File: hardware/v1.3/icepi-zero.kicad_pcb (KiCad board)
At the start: 4 copper layers, 65 x 30 mm, 161 parts, among them J1 Conn_02x20_Counter_Clockwise, J2 HDMI_C_1.3, J3 USB_C_Receptacle_USB2.0_14P, J4 USB_C_Receptacle_USB2.0_14P, J5 USB_C_Receptacle_USB2.0_14P, J6 Micro_SD_Card_Det2, SW1 SW_Push, SW2 SW_Push, U1 ECP5-CABGA256, U10 W9825G6KH, U11 W25Q128JVS, U2 TLV62569DBV, U3 TLV62569DBV, U4 TLV62569DBV, U5 PCA9306DC1, U6 FT231XQ, U7 TPD2EUSB30A, U8 TPD2EUSB30A, U9 TPD2EUSB30A, Y1 SG-8018CG 50.000000MHz

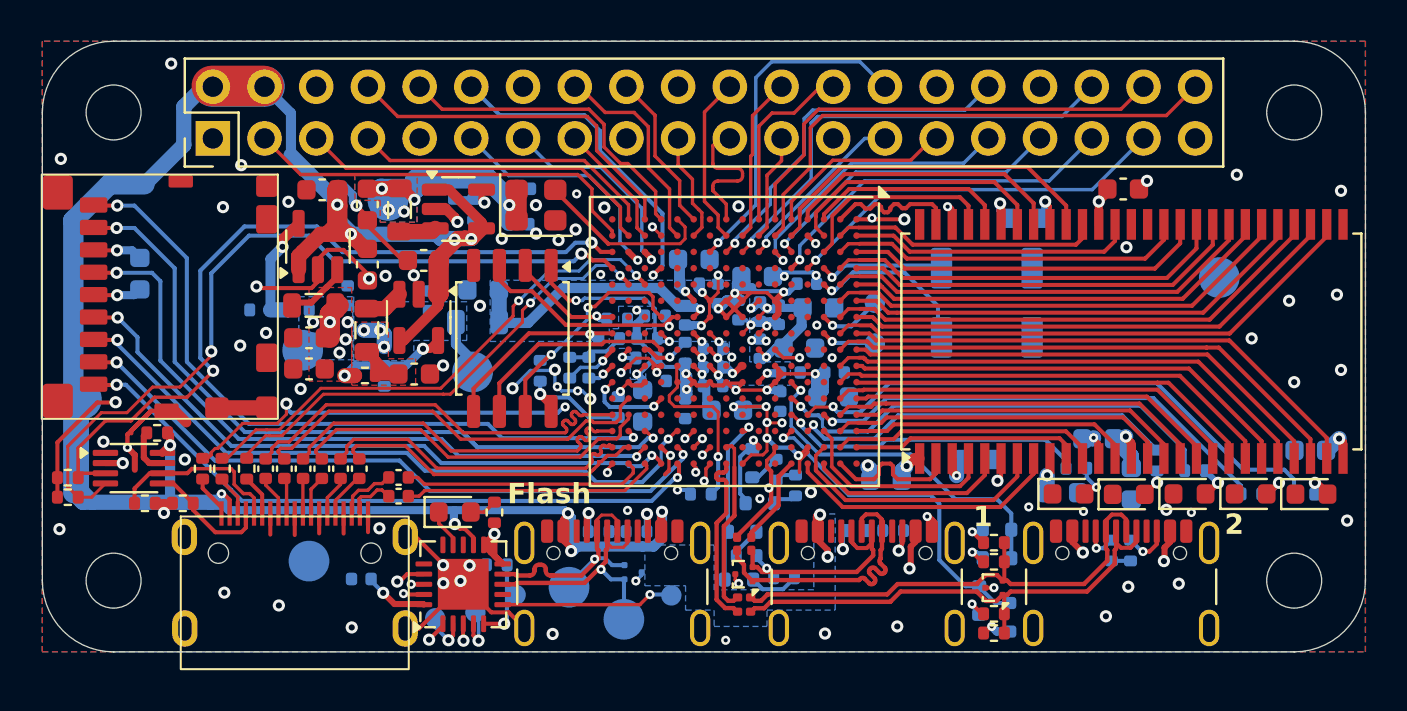
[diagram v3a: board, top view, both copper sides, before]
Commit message: Added start of documentation and changed GPDI
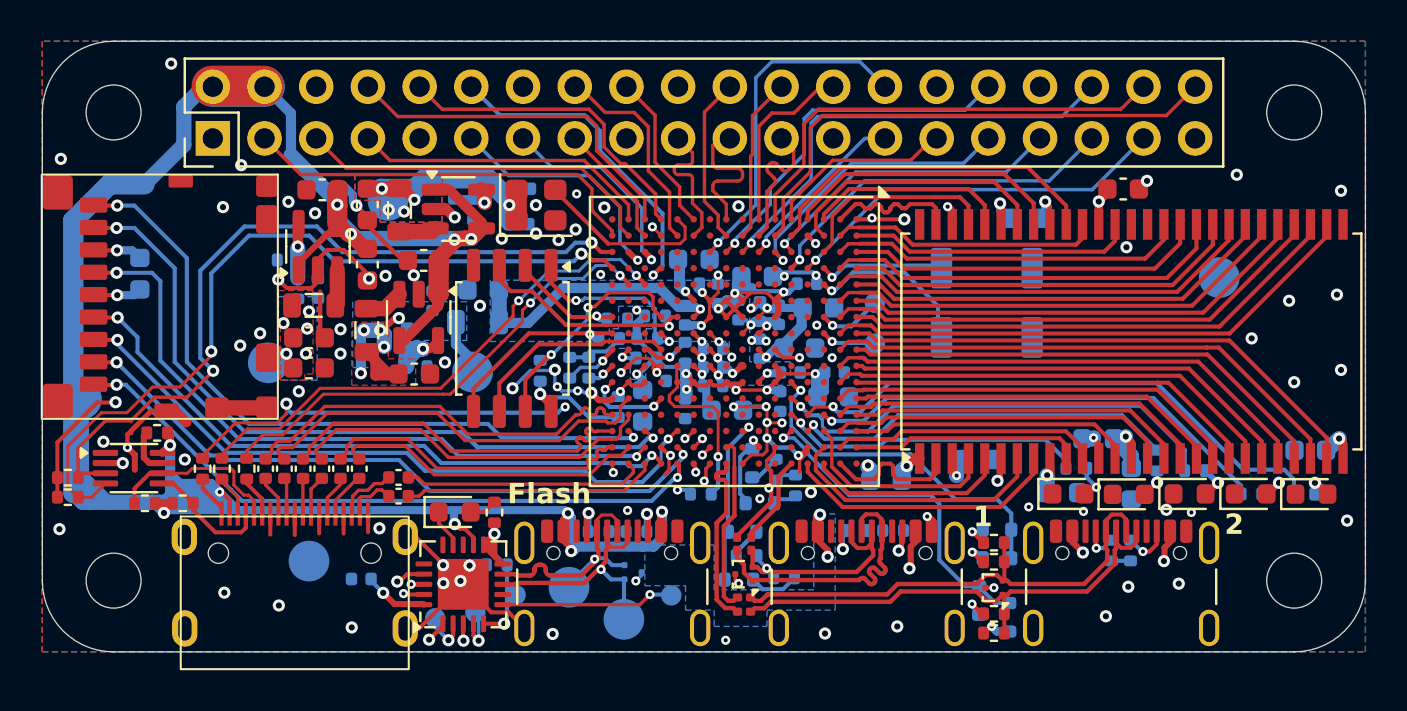
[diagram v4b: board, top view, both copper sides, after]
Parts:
- added REF**: CE-Logo_8.5x6mm_SilkScreen, Symbol:CE-Logo_8.5x6mm_SilkScreen, B.Cu at (126.6, 99.5)
- J2: value HDMI_C_1.3 -> GPDI_C_1.3
- R8: moved to B.Cu
- moved R7 2.80 mm to (128.1, 100.8)
- moved R8 2.77 mm to (133.9, 104.6), turned to -90 degrees
- moved TP6 1.80 mm to (127.1, 105.8)
- moved R9 1.65 mm to (134.4, 106.0), turned to 0 degrees
- moved C7 1.50 mm to (129.5, 102.1)
- moved R6 1.05 mm to (128.6, 102.2), turned to 90 degrees
- moved C19 0.17 mm to (135.2, 102.8)
- turned C6 to 0 degrees
- turned C5 to 0 degrees
- turned L1 to 180 degrees
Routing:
- net +5V: track 172.3 -> 189.5 mm
- net +2V5: track 8.96 -> 12.3 mm, vias 3 -> 5
- net Net-(U2-FB): track 5.70 -> 2.57 mm
- net +1V1: track 40.8 -> 38.3 mm
- net Net-(U3-FB): track 5.80 -> 3.96 mm, vias 2 -> 1
- net /GPIO11: track 5.24 -> 7.00 mm
- net /GPIO10: track 5.42 -> 6.85 mm
- net GND: track 98.4 -> 99.5 mm, vias 108 -> 111
- net Net-(U2-SW): track 2.62 -> 1.80 mm
- net /GPDI/GPDI_CLK-: track 20.5 -> 19.9 mm

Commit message: DVI multires
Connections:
- U1 pad M11: /USB/JTAG_TDO -> unconnected-(U1E-PR47A/+/HS/RSQ44-PadM11)
- U1 pad N12: /USB/JTAG_TMS -> unconnected-(U1E-PR44D/-/RSQ44-PadN12)
- U1 pad P11: /USB/JTAG_TDI -> unconnected-(U1E-PR47C/+/RSQ44/LRC_GPLL0T_IN-PadP11)
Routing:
- net /USB/JTAG_TDI: track 32.6 -> 31.7 mm
- net /USB/JTAG_TMS: track 34.5 -> 34.0 mm
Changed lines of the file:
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@@
 	(net 259 "/GPIO27")
 	(net 260 "unconnected-(U1J-PB18A{slash}WRITEN-PadM9)")
+	(net 261 "unconnected-(U1E-PR44D{slash}-{slash}RSQ44-PadN12)")
+	(net 262 "unconnected-(U1E-PR47C{slash}+{slash}RSQ44{slash}LRC_GPLL0T_IN-PadP11)")
+	(net 263 "unconnected-(U1E-PR47A{slash}+{slash}HS{slash}RSQ44-PadM11)")
 	(footprint "MountingHole:MountingHole_2.7mm_M2.5"
 		(layer "F.Cu")
@@
 			(property pad_prop_bga)
 			(layers "F.Cu" "F.Mask" "F.Paste")
-			(net 5 "/USB/JTAG_TDO")
+			(net 263 "unconnected-(U1E-PR47A{slash}+{slash}HS{slash}RSQ44-PadM11)")
 			(pinfunction "PR47A/+/HS/RSQ44")
 			(pintype "bidirectional")
@@
 			(property pad_prop_bga)
 			(layers "F.Cu" "F.Mask" "F.Paste")
-			(net 8 "/USB/JTAG_TMS")
+			(net 261 "unconnected-(U1E-PR44D{slash}-{slash}RSQ44-PadN12)")
 			(pinfunction "PR44D/-/RSQ44")
 			(pintype "bidirectional")
@@
 			(property pad_prop_bga)
 			(layers "F.Cu" "F.Mask" "F.Paste")
-			(net 4 "/USB/JTAG_TDI")
+			(net 262 "unconnected-(U1E-PR47C{slash}+{slash}RSQ44{slash}LRC_GPLL0T_IN-PadP11)")
 			(pinfunction "PR47C/+/RSQ44/LRC_GPLL0T_IN")
 			(pintype "bidirectional")
@@
 		(net 4)
 	)
-	(segment
-		(start 144.96 106.91)
-		(end 144.8 106.75)
-		(width 0.2)
-		(layer "F.Cu")
-		(net 4)
-	)
-	(segment
-		(start 145.44 106.91)
-		(end 144.96 106.91)
-		(width 0.2)
-		(layer "F.Cu")
-		(net 4)
-	)
-	(segment
-		(start 145.6 106.75)
-		(end 145.44 106.91)
-		(width 0.2)
-		(layer "F.Cu")
-		(net 4)
-	)
 	(via
 		(at 144.399998 107.209961)
@@
 	)
 	(segment
-		(start 148.931745 107.95)
-		(end 149.199998 108.218253)
+		(start 147.19 105.95)
+		(end 146.8 106.34)
 		(width 0.15)
 		(layer "F.Cu")
@@
 	)
 	(segment
-		(start 149.199998 108.218253)
-		(end 149.199999 110.40996)
+		(start 148.931745 107.95)
+		(end 149.199998 108.218253)
 		(width 0.15)
 		(layer "F.Cu")
@@
 	)
 	(segment
-		(start 146.8 107.681745)
-		(end 147.068255 107.95)
+		(start 146.8 106.34)
+		(end 146.8 107.681745)
 		(width 0.15)
 		(layer "F.Cu")
@@
 	)
 	(segment
-		(start 145.85 117.185)
-		(end 145.355 117.68)
-		(width 0.17)
-		(layer "F.Cu")
-		(net 5)
-	)
-	(segment
-		(start 147.2 107)
-		(end 146.8 107.4)
+		(start 146.8 107.681745)
+		(end 147.068255 107.95)
 		(width 0.15)
 		(layer "F.Cu")
@@
 	)
 	(segment
-		(start 146.8 107.4)
-		(end 146.8 107.681745)
-		(width 0.15)
+		(start 145.85 117.185)
+		(end 145.355 117.68)
+		(width 0.17)
 		(layer "F.Cu")
 		(net 5)
@@
 	)
 	(segment
-		(start 147.2 106.75)
-		(end 147.2 107)
+		(start 147.2 105.95)
+		(end 147.19 105.95)
 		(width 0.15)
 		(layer "F.Cu")
@@
 	)
 	(segment
-		(start 147.165 105.985)
-		(end 147.165 106.715)
+		(start 149.199998 108.218253)
+		(end 149.199999 110.40996)
 		(width 0.15)
 		(layer "F.Cu")
@@
 		(net 8)
 	)
-	(segment
-		(start 146.4 107.580151)
-		(end 146.044151 107.936)
-		(width 0.2)
-		(layer "F.Cu")
-		(net 8)
-	)
 	(via
 		(at 146.044151 107.936)
@@
 		(net 259)
 	)
+	(segment
+		(start 147.2 106.75)
+		(end 147.09 106.75)
+		(width 0.15)
+		(layer "F.Cu")
+		(net 263)
+	)
 	(zone
